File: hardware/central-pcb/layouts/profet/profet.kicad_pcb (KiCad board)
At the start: 2 copper layers, 58 parts

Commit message: docs: add logic audit and reference datasheets
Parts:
- removed J17, J18, J19, J20: , central-pcb:PinSocket_1x02_P2.54mm_Vertical
- removed J21: , central-pcb:TerminalBlock_Phoenix_MPT-0,5-4-2.54_1x04_P2.54mm_Horizontal
- removed J22: , central-pcb:TerminalBlock_Phoenix_MPT-0,5-2-2.54_1x02_P2.54mm_Horizontal
- removed Q3, Q4, Q6: , central-pcb:SOT-23
- removed Q5: , central-pcb:SOIC-8_3.9x4.9mm_P1.27mm
- added R19: , central-pcb:R_0805_2012Metric, F.Cu at (90.0, 70.0)
- added R20: , central-pcb:R_0805_2012Metric, F.Cu at (102.0, 70.0)
- added R21: , central-pcb:R_0805_2012Metric, F.Cu at (90.0, 80.0)
- added R22: , central-pcb:R_0805_2012Metric, F.Cu at (90.0, 110.0)
- added R23: , central-pcb:R_0805_2012Metric, F.Cu at (102.0, 110.0)
- added R24: , central-pcb:R_0805_2012Metric, F.Cu at (90.0, 120.0)
- added R25: , central-pcb:R_0805_2012Metric, F.Cu at (90.0, 150.0)
- added R26: , central-pcb:R_0805_2012Metric, F.Cu at (102.0, 150.0)
- added R27: , central-pcb:R_0805_2012Metric, F.Cu at (90.0, 160.0)
- added R28: , central-pcb:R_0805_2012Metric, F.Cu at (260.0, 138.0)
- added R29: , central-pcb:R_0805_2012Metric, F.Cu at (150.0, 30.0)
- added R30: , central-pcb:R_0805_2012Metric, F.Cu at (162.0, 30.0)
- added R31: , central-pcb:R_0805_2012Metric, F.Cu at (150.0, 40.0)
- added R32: , central-pcb:R_0805_2012Metric, F.Cu at (275.0, 138.0)
- added R33: , central-pcb:R_0805_2012Metric, F.Cu at (218.0, 160.0)
- added R34: , central-pcb:R_0805_2012Metric, F.Cu at (226.0, 160.0)
- added U10: , central-pcb:SOIC-14-1EP_3.9x8.7mm_P1.27mm_EP4.3x4.7mm, F.Cu at (162.0, 40.0)
- added U7: , central-pcb:SOIC-14-1EP_3.9x8.7mm_P1.27mm_EP4.3x4.7mm, F.Cu at (102.0, 80.0)
- added U8: , central-pcb:SOIC-14-1EP_3.9x8.7mm_P1.27mm_EP4.3x4.7mm, F.Cu at (102.0, 120.0)
- added U9: , central-pcb:SOIC-14-1EP_3.9x8.7mm_P1.27mm_EP4.3x4.7mm, F.Cu at (102.0, 160.0)
- J15: footprint central-pcb:PinSocket_1x05_P2.54mm_Vertical -> central-pcb:TerminalBlock_Phoenix_MPT-0,5-4-2.54_1x04_P2.54mm_Horizontal
- J16: footprint central-pcb:PinSocket_1x02_P2.54mm_Vertical -> central-pcb:TerminalBlock_Phoenix_MPT-0,5-2-2.54_1x02_P2.54mm_Horizontal
- Q2: footprint central-pcb:SOT-23 -> central-pcb:SOIC-8_3.9x4.9mm_P1.27mm
- U1, U2, U3, U6: footprint central-pcb:SOT-223 -> central-pcb:SOIC-14-1EP_3.9x8.7mm_P1.27mm_EP4.3x4.7mm
- moved R16 221.0 mm to (90.0, 30.0)
- moved J15 189.7 mm to (275.0, 90.0), turned to 0 degrees
- moved J16 147.7 mm to (260.0, 102.0), turned to 0 degrees
- moved R9 143.1 mm to (150.0, 160.0)
- moved R7 133.8 mm to (150.0, 150.0)
- moved R13 127.8 mm to (218.0, 40.0)
- moved C1 121.8 mm to (210.0, 160.0)
- moved Q2 109.3 mm to (222.0, 30.0)
- moved R10 103.2 mm to (275.0, 126.0)
- moved R17 90.0 mm to (102.0, 30.0), turned to 0 degrees
- moved R11 89.0 mm to (210.0, 130.0)
- moved R18 82.7 mm to (90.0, 40.0), turned to 0 degrees
- moved U6 70.0 mm to (102.0, 40.0)
- moved R15 69.3 mm to (210.0, 90.0)
- moved Q1 67.3 mm to (210.0, 30.0)
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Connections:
- C1 pad 2: 2 -> gnd
- D1 pad 2: 2 -> gnd
- D2 pad 2: 2 -> gnd
- D3 pad 2: 2 -> gnd
- D4 pad 2: 2 -> gnd
- D5 pad 2: 2 -> gnd
- J1 pad 2: 2 -> gnd
- J11 pad 1: out1_neg -> power_out-3
- J11 pad 2: 2 -> power_in
- J11 pad 4: power_in -> gnd
- J12 pad 1: out2_neg -> power_out-4
- J12 pad 2: 2 -> power_in
- J12 pad 4: power_in -> gnd
- J13 pad 1: out3_neg -> power_out-5
- J13 pad 2: 2 -> power_in
- J13 pad 4: power_in -> gnd
- J14 pad 1: out4_neg -> power_out-6
- J14 pad 2: 2 -> power_in
- J14 pad 4: power_in -> gnd
- J15 pad 1: 2 -> 1-4
- J15 pad 2: GPIO12 -> power_in
- J15 pad 3: GPIO13 -> pump_terminal-3
- J15 pad 4: GPIO14 -> gnd
- J16 pad 1: out1_pos -> power_in
- J16 pad 2: out1_neg -> gnd
- J2 pad 2: 2 -> gnd
- J3 pad 2: 2 -> gnd
- J4 pad 2: 2 -> gnd
- J5 pad 2: 2 -> gnd
- J7 pad 18: GPIO12 -> control-4
- J7 pad 19: GPIO13 -> control-5
- J7 pad 2: esp32.left_header-2 -> 2
- J7 pad 20: GPIO14 -> control-6
- J7 pad 22: 2 -> gnd
- J7 pad 4: control-6 -> control-10
- J7 pad 8: GPIO15 -> control-7
- J8 pad 19: control-5 -> control-9
- J8 pad 2: 2 -> gnd
- J8 pad 21: control-4 -> control-8
- J8 pad 22: 2 -> gnd
- J9 pad 2: 2 -> gnd
- Q1 pad 2: 2 -> gnd
- Q2 pad 1: aux2_stage-gate -> power_in
- Q2 pad 2: 2 -> power_in
- Q2 pad 3: aux2_stage-drain -> power_in
- R1 pad 2: gate -> input
- R10 pad 1: control-4 -> 1
- R10 pad 2: 2 -> anode
- R11 pad 1: fan_stage-drain -> control-3
- R11 pad 2: power_in -> dcdc_opto-anode
- R12 pad 1: control-5 -> control-8
- R12 pad 2: inverter_opto-anode -> gate
- R13 pad 1: 1-2 -> control-8
- R13 pad 2: anode-1 -> gnd
- R14 pad 1: control-6 -> drain
- R14 pad 2: pump_stage-gate -> power_in
- R15 pad 1: control-6 -> control-9
- R15 pad 2: 2 -> inverter_opto-anode
- R16 pad 1: 1-1 -> control-4
- R16 pad 2: anode-2 -> led_zone1_stage-input
- R17 pad 1: power_in -> control-4
- R17 pad 2: v_out -> gnd
- R18 pad 1: v_out -> led_zone1_stage-current_sense
- R18 pad 2: 2 -> gnd
- R2 pad 2: 2 -> gnd
- R3 pad 1: control-1 -> current_sense
- R3 pad 2: aux2_stage-gate -> gnd
- R4 pad 2: 2 -> aux2_stage-input
- R5 pad 1: control-2 -> control-1
- R5 pad 2: aux3_stage-gate -> gnd
- R6 pad 1: control-2 -> aux2_stage-current_sense
- R6 pad 2: 2 -> gnd
- R7 pad 1: 1 -> control-2
- R7 pad 2: anode -> aux3_stage-input
- R8 pad 1: control-3 -> control-2
- R8 pad 2: dcdc_opto-anode -> gnd
- R9 pad 1: control-4 -> aux3_stage-current_sense
- R9 pad 2: fan_stage-gate -> gnd
- U1 pad 1: drain -> (no net)
- U1 pad 2: power_in -> (no net)
- U1 pad 3: power_out -> gnd
- U1 pad 4: power_in -> input
- U2 pad 1: aux2_stage-drain -> (no net)
- U2 pad 2: power_in -> (no net)
- U2 pad 3: power_out-1 -> gnd
- U2 pad 4: power_in -> aux2_stage-input
- U3 pad 1: aux3_stage-drain -> (no net)
- U3 pad 2: power_in -> (no net)
- U3 pad 3: power_out-2 -> gnd
- U3 pad 4: power_in -> aux3_stage-input
- U4 pad 2: 2 -> gnd
- U5 pad 2: 2 -> gnd
- U6 pad 1: pump_stage-drain -> (no net)
- U6 pad 2: power_in -> (no net)
- U6 pad 3: 1-4 -> gnd
- U6 pad 4: power_in -> led_zone1_stage-input

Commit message: fix(central): resolve GPIO19/20 USB-JTAG conflict and align firmware pin mappings (H-01, FC-01)
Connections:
- J7 pad 10: GPIO17 -> control-8
- J7 pad 11: GPIO18 -> control-3
- J8 pad 20: control-3 -> GPIO20
- J8 pad 21: control-8 -> GPIO19
- J8 pad 7: 7 -> (no net)
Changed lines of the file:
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@@
 	(net 11 "aux3_stage-current_sense")
 	(net 12 "anode")
-	(net 13 "control-3")
+	(net 13 "GPIO20")
 	(net 14 "dcdc_opto-anode")
 	(net 15 "out_emitter")
 	(net 16 "out_collector")
-	(net 17 "GPIO17")
-	(net 18 "GPIO18")
 	(net 19 "12")
 	(net 20 "13")
@@
 	(net 42 "18")
 	(net 43 "control-9")
-	(net 44 "control-8")
+	(net 44 "GPIO19")
 	(net 45 "esp32.right_header-3")
 	(net 46 "4")
@@
 	(net 83 "anode-2")
 	(net 84 "v_out")
+	(net 85 "control-3")
+	(net 86 "control-8")
 	(footprint "central-pcb:TerminalBlock_Phoenix_MPT-0,5-2-2.54_1x02_P2.54mm_Horizontal"
 		(layer "F.Cu")
@@
 			(layers "*.Cu" "*.Mask")
 			(remove_unused_layers no)
-			(net 17 "GPIO17")
+			(net 86 "control-8")
 		)
 		(pad "11" thru_hole circle
@@
 			(layers "*.Cu" "*.Mask")
 			(remove_unused_layers no)
-			(net 18 "GPIO18")
+			(net 85 "control-3")
 		)
 		(pad "12" thru_hole circle
@@
 			(layers "*.Cu" "*.Mask")
 			(remove_unused_layers no)
-			(net 48 "7")
+			(net 0 "")
 		)
 		(pad "8" thru_hole circle
@@
 			(layers "*.Cu" "*.Mask")
 			(remove_unused_layers no)
-			(net 13 "control-3")
+			(net 13 "GPIO20")
 		)
 		(pad "21" thru_hole circle
@@
 			(layers "*.Cu" "*.Mask")
 			(remove_unused_layers no)
-			(net 44 "control-8")
+			(net 44 "GPIO19")
 		)
 		(pad "22" thru_hole circle
@@
 			(size 1.025 1.4)
 			(layers "F.Cu" "F.Mask" "F.Paste")
-			(net 44 "control-8")
+			(net 86 "control-8")
 			(roundrect_rratio 0.243902)
 		)
@@
 			(size 1.025 1.4)
 			(layers "F.Cu" "F.Mask" "F.Paste")
-			(net 44 "control-8")
+			(net 86 "control-8")
 			(roundrect_rratio 0.243902)
 		)
@@
 			(size 1.025 1.4)
 			(layers "F.Cu" "F.Mask" "F.Paste")
-			(net 13 "control-3")
+			(net 85 "control-3")
 			(roundrect_rratio 0.243902)
 		)

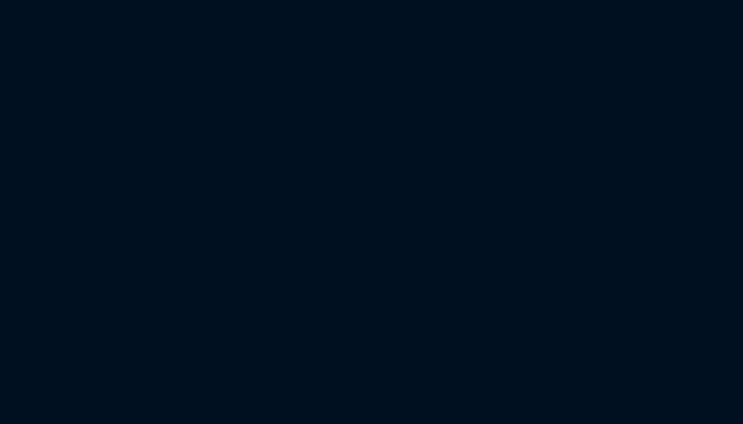
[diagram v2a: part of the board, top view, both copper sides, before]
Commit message: fix(central): correct battery telemetry divider ratio, use analogReadMilliVolts and add Zener protection (FC-03, H-07)
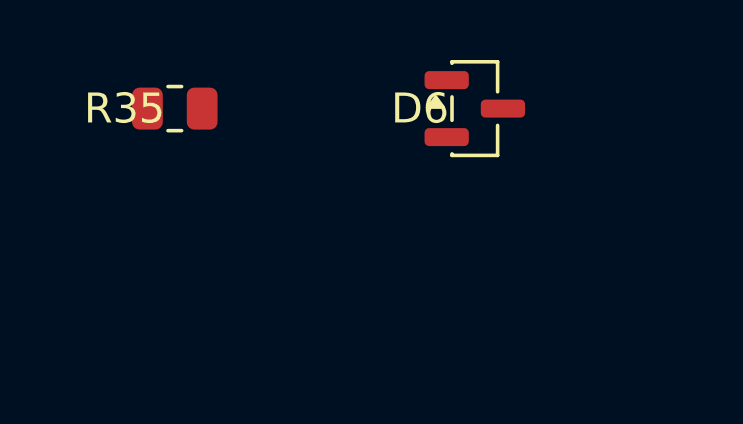
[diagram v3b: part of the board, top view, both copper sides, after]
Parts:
- added D6: , central-pcb:SOT-23, F.Cu at (10.0, 0.00)
- added R35: , central-pcb:R_0805_2012Metric, F.Cu at (0.00, 0.00)
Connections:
- C1 pad 1: v_out -> voltage_sensor-1
- J8 pad 7: (no net) -> 7
- R33 pad 2: v_out -> voltage_sensor-1
- R34 pad 1: v_out -> voltage_sensor-1

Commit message: fix(hardware): connect pump flyback diode to override terminal output pin to protect switch contacts (H-06)
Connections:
- D4 pad 1: 1-4 -> cathode
- J15 pad 1: 1-4 -> power_out-7
- J15 pad 3: pump_terminal-3 -> cathode
- U10 pad 10: 1-4 -> power_out-7
- U10 pad 11: 1-4 -> power_out-7
- U10 pad 12: 1-4 -> power_out-7
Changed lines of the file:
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@@
 	(net 76 "anode-1")
 	(net 77 "1-2")
-	(net 78 "1-4")
+	(net 78 "power_out-7")
 	(net 79 "control-10")
 	(net 80 "pump_stage-input")
 	(net 81 "pump_stage-current_sense")
-	(net 82 "pump_terminal-3")
 	(net 83 "anode-2")
 	(net 85 "control-3")
@@
 	(net 18 "7")
 	(net 87 "voltage_sensor-1")
+	(net 48 "cathode")
 	(footprint "central-pcb:TerminalBlock_Phoenix_MPT-0,5-2-2.54_1x02_P2.54mm_Horizontal"
 		(layer "F.Cu")
@@
 			(size 1.95 0.6)
 			(layers "F.Cu" "F.Mask" "F.Paste")
-			(net 78 "1-4")
+			(net 78 "power_out-7")
 			(roundrect_rratio 0.25)
 		)
@@
 			(size 1.95 0.6)
 			(layers "F.Cu" "F.Mask" "F.Paste")
-			(net 78 "1-4")
+			(net 78 "power_out-7")
 			(roundrect_rratio 0.25)
 		)
@@
 			(size 1.95 0.6)
 			(layers "F.Cu" "F.Mask" "F.Paste")
-			(net 78 "1-4")
+			(net 78 "power_out-7")
 			(roundrect_rratio 0.25)
 		)
@@
 			(layers "*.Cu" "*.Mask")
 			(remove_unused_layers no)
-			(net 78 "1-4")
+			(net 48 "cathode")
 			(roundrect_rratio 0.078125)
 		)
@@
 			(layers "*.Cu" "*.Mask")
 			(remove_unused_layers no)
-			(net 78 "1-4")
+			(net 78 "power_out-7")
 			(roundrect_rratio 0.113636)
 		)
@@
 			(layers "*.Cu" "*.Mask")
 			(remove_unused_layers no)
-			(net 82 "pump_terminal-3")
+			(net 48 "cathode")
 		)
 		(pad "4" thru_hole circle
@@
 		)
 		(pad "1" smd roundrect
-			(at -0.9125 0 0)
+			(at -0.9125 0)
 			(size 1.025 1.4)
 			(layers "F.Cu" "F.Mask" "F.Paste")
@@
 		)
 		(pad "2" smd roundrect
-			(at 0.9125 0 0)
+			(at 0.9125 0)
 			(size 1.025 1.4)
 			(layers "F.Cu" "F.Mask" "F.Paste")
@@
 		)
 		(pad "1" smd roundrect
-			(at -0.9375 -0.95 0)
+			(at -0.9375 -0.95)
 			(size 1.475 0.6)
 			(layers "F.Cu" "F.Mask" "F.Paste")
@@
 		)
 		(pad "2" smd roundrect
-			(at -0.9375 0.95 0)
+			(at -0.9375 0.95)
 			(size 1.475 0.6)
 			(layers "F.Cu" "F.Mask" "F.Paste")
@@
 		)
 		(pad "3" smd roundrect
-			(at 0.9375 0 0)
+			(at 0.9375 0)
 			(size 1.475 0.6)
 			(layers "F.Cu" "F.Mask" "F.Paste")

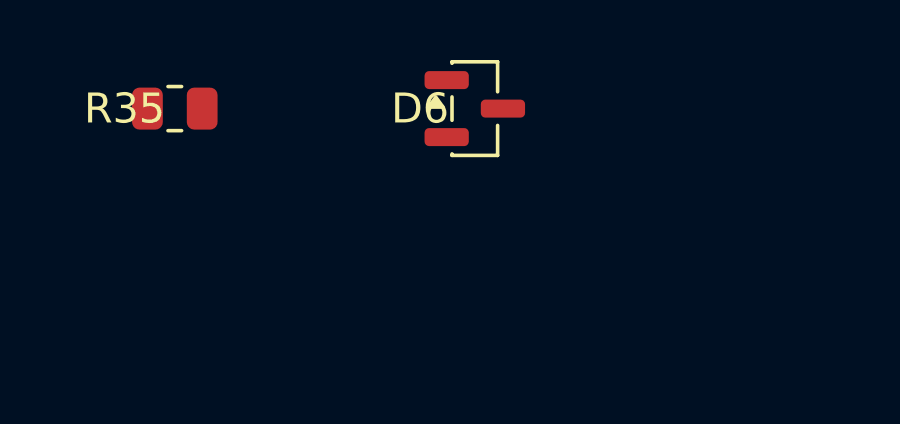
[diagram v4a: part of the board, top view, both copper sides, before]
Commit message: feat(hardware): update central PCB layout and Atopile definitions
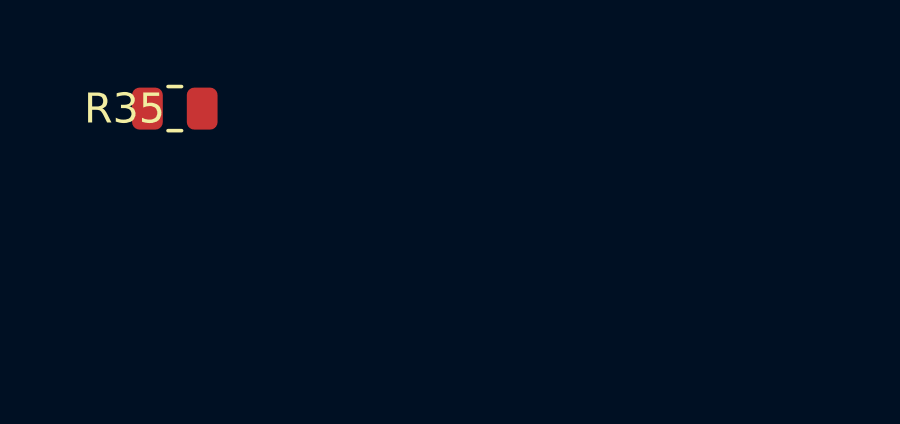
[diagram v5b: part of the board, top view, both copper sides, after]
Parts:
- removed D6: , central-pcb:SOT-23
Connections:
- net GPIO20 renamed 20
- J7 pad 21: 21 -> v_mcu_5v
- J8 pad 1: v_mcu_5v -> gnd
- J8 pad 18: 18 -> control-9
- J8 pad 19: control-9 -> 19
- J8 pad 2: gnd -> esp32.right_header-2
- J8 pad 21: GPIO19 -> gnd
- J8 pad 4: 4 -> v_out
- J8 pad 5: v_out -> 1
- J8 pad 6: 1 -> 6

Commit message: feat(hardware): implement automated KiCad 3D PCB rendering and STEP CAD export
- Add headless PCB rendering script (hardware/central-pcb/scripts/render_pcb.py) supporting both native kicad-cli and Flatpak org.kicad.KiCad.
- Add clean Edge.Cuts board outline and 4x M3 corner mounting holes to profet and modular PCB layouts.
- Fix series resistor coordinates (R35 and R6) from unplaced origin (0,0) to analog divider cluster at (234,160).
- Generate high-resolution 1440p raytraced 3D isometric and orthographic renders, silkscreen vector graphics, and 3D STEP models.
- Create engineering reference guide (.agents/skills/schematic-design/references/pcb_rendering_and_visualization.md) and link in SKILL.md and docs/README.md.
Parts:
- moved R35 283.5 mm to (234.0, 160.0)
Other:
- board outline added: 274 x 154 mm
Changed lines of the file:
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@@
 	(footprint "central-pcb:R_0805_2012Metric"
 		(layer "F.Cu")
-		(at 0 0 0)
+		(at 234 160 0)
 		(descr "Resistor SMD 0805 (2012 Metric), square (rectangular) end terminal, IPC-7351 nominal, (Body size source: IPC-SM-782 page 72, https://www.pcb-3d.com/wordpress/wp-content/uploads/ipc-sm-782a_amendment_1_and_2.pdf)")
 		(tags "resistor")
@@
 		)
 	)
+	(gr_circle
+		(center 24 24)
+		(end 25.6 24)
+		(stroke
+			(width 0.15)
+			(type solid)
+		)
+		(fill none)
+		(layer "Edge.Cuts")
+		(uuid "00000000-edge-cuts-hole-000000000001")
+	)
+	(gr_circle
+		(center 286 24)
+		(end 287.6 24)
+		(stroke
+			(width 0.15)
+			(type solid)
+		)
+		(fill none)
+		(layer "Edge.Cuts")
+		(uuid "00000000-edge-cuts-hole-000000000002")
+	)
+	(gr_circle
+		(center 24 166)
+		(end 25.6 166)
+		(stroke
+			(width 0.15)
+			(type solid)
+		)
+		(fill none)
+		(layer "Edge.Cuts")
+		(uuid "00000000-edge-cuts-hole-000000000003")
+	)
+	(gr_circle
+		(center 286 166)
+		(end 287.6 166)
+		(stroke
+			(width 0.15)
+			(type solid)
+		)
+		(fill none)
+		(layer "Edge.Cuts")
+		(uuid "00000000-edge-cuts-hole-000000000004")
+	)
+	(gr_rect
+		(start 18 18)
+		(end 292 172)
+		(stroke
+			(width 0.15)
+			(type solid)
+		)
+		(fill none)
+		(layer "Edge.Cuts")
+		(uuid "00000000-edge-cuts-rect-000000000001")
+	)
 )

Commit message: feat(hardware): physical layout, procedural routing, 0 DRC violations and 3D CAD models for central-pcb
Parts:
- removed J2, J3: , central-pcb:TerminalBlock_Phoenix_MPT-0,5-2-2.54_1x02_P2.54mm_Horizontal
- removed R4, R5, R6, R7, R8, R9: , central-pcb:R_0805_2012Metric
- removed U2, U3: , central-pcb:SOIC-14-1EP_3.9x8.7mm_P1.27mm_EP4.3x4.7mm
- moved J16 348.5 mm to (-60.0, -36.0), turned to 180 degrees
- moved J11 334.4 mm to (-58.0, 35.0)
- moved R32 323.7 mm to (-17.0, -1.68), turned to 180 degrees
- moved R28 319.9 mm to (-17.0, -22.0), turned to 180 degrees
- moved J12 305.0 mm to (-42.0, 35.0)
- moved J13 304.1 mm to (-26.0, 35.0)
- moved R10 292.5 mm to (17.0, -11.8)
- moved D3 289.2 mm to (-22.0, -22.0), turned to 180 degrees
- moved D5 287.4 mm to (-22.0, -1.68), turned to 180 degrees
- moved J6 283.9 mm to (34.0, -36.0), turned to 180 degrees
- moved R35 278.4 mm to (17.0, -14.4), turned to 180 degrees
- moved R34 267.7 mm to (26.0, -18.0)
- moved R33 264.8 mm to (22.0, -18.0), turned to -90 degrees
- moved C1 253.1 mm to (30.0, -18.0)
- moved U4 249.6 mm to (26.4, -25.0)
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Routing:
- net power_in: track 0.00 -> 491.5 mm, vias 0 -> 2
- net gnd: track 0.00 -> 126.6 mm, vias 0 -> 60
- net v_mcu_5v: track 0.00 -> 94.5 mm
- net control: track 0.00 -> 94.2 mm, vias 0 -> 4
- net control-9: track 0.00 -> 93.5 mm, vias 0 -> 1
- net control-4: track 0.00 -> 77.6 mm, vias 0 -> 1
- net control-10: track 0.00 -> 77.0 mm, vias 0 -> 2
- net control-8: track 0.00 -> 70.2 mm
- net control-5: track 0.00 -> 62.1 mm, vias 0 -> 1
- net control-3: track 0.00 -> 61.2 mm, vias 0 -> 2
- net control-7: track 0.00 -> 52.0 mm, vias 0 -> 2
- net control-6: track 0.00 -> 46.6 mm, vias 0 -> 1
- net 1-3: track 0.00 -> 27.7 mm
- net power_out-7: track 0.00 -> 21.1 mm
- net power_out-4: track 0.00 -> 21.1 mm
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- added copper zone on B.Cu, net gnd
- added copper zone on F.Cu, net gnd
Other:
- board size 274 x 154 mm -> 150 x 95 mm
